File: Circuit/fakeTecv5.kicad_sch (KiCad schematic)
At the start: 70 parts, among them J1 EXTRA, J11 FET1 3,3, J12 FET2 3,3, J13 FET3 3,3, J14 GPS Pins, J16 Encoder Pads, J37 SCL, J38 JST-SH-4, J39 SDA, J40 3.3V, J41 GND, J42 FET1, J43 FET2, J44 FET3, J45 GND, J46 3.3V, J47 GND, J48 GND, J49 GND, J5 I2C Oled screen, J6 FET1 Drain, J7 FET2 Drain, J8 FET3 Drain, J9 JST-PH-2, Q1 AO3400A, Q2 AO3400A, Q3 AO3400A, SW1 Reset, SW2 SW_Push, U1 XB8089D0, U2 HT-RA62, U3 nice!nano v2

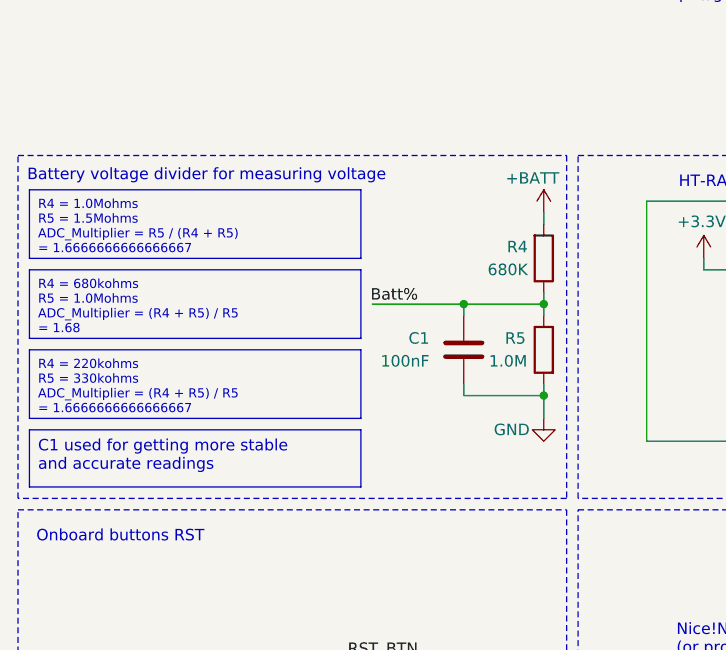
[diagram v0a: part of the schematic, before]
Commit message: improve documentation of battery voltage divider ratio
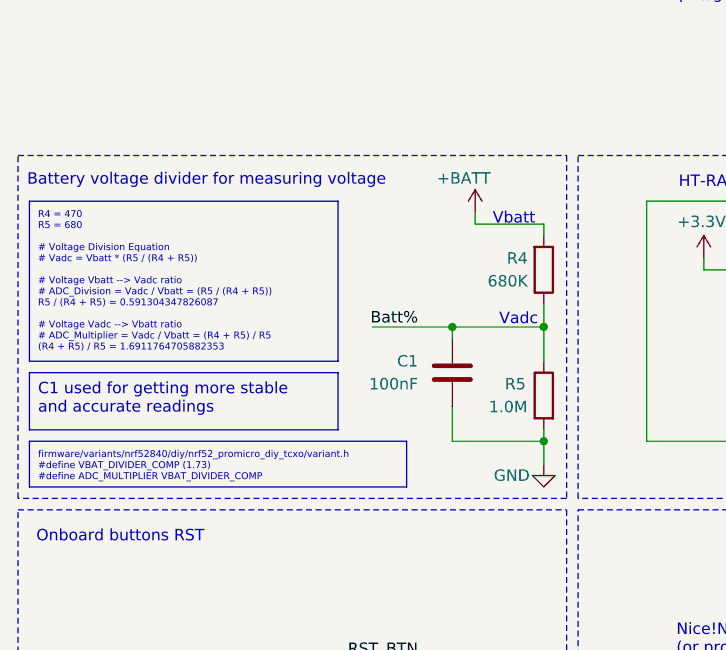
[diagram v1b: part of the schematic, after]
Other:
- note added: "Vadc"
- note added: "Vbatt"
- moved on the sheet: C1, R4, R5

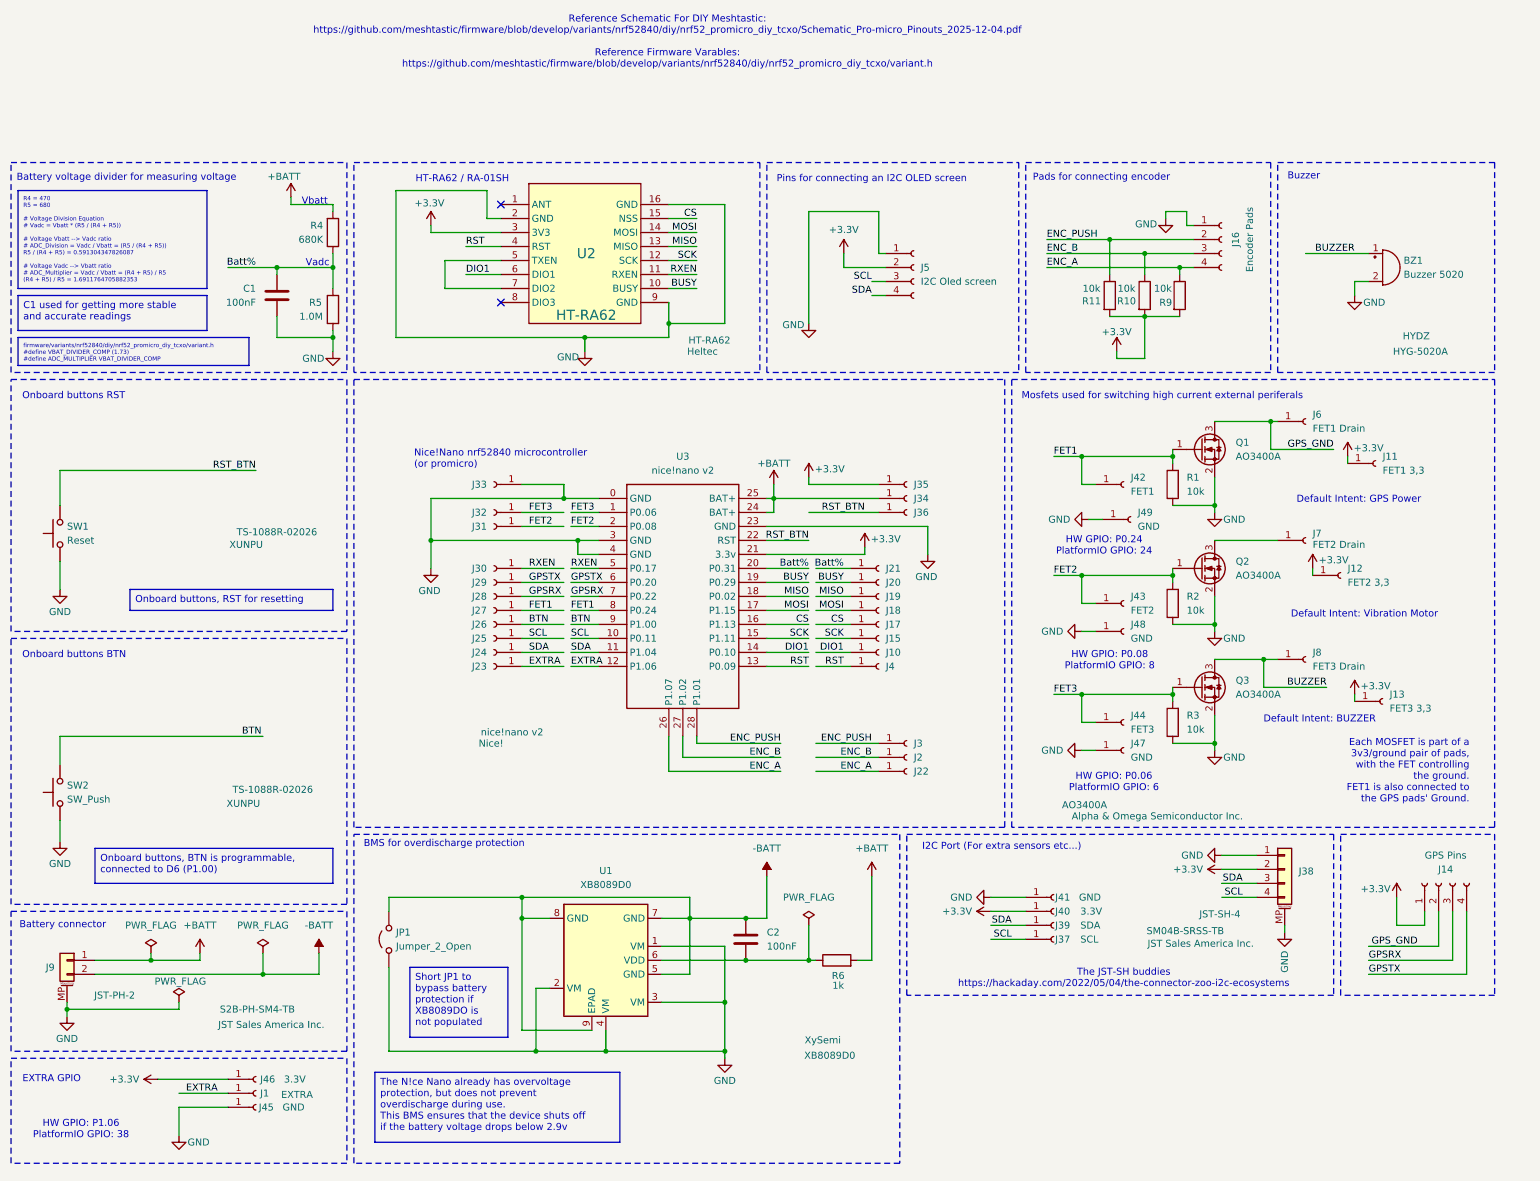
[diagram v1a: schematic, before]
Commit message: bom update and added extra power pads for easier adjustments
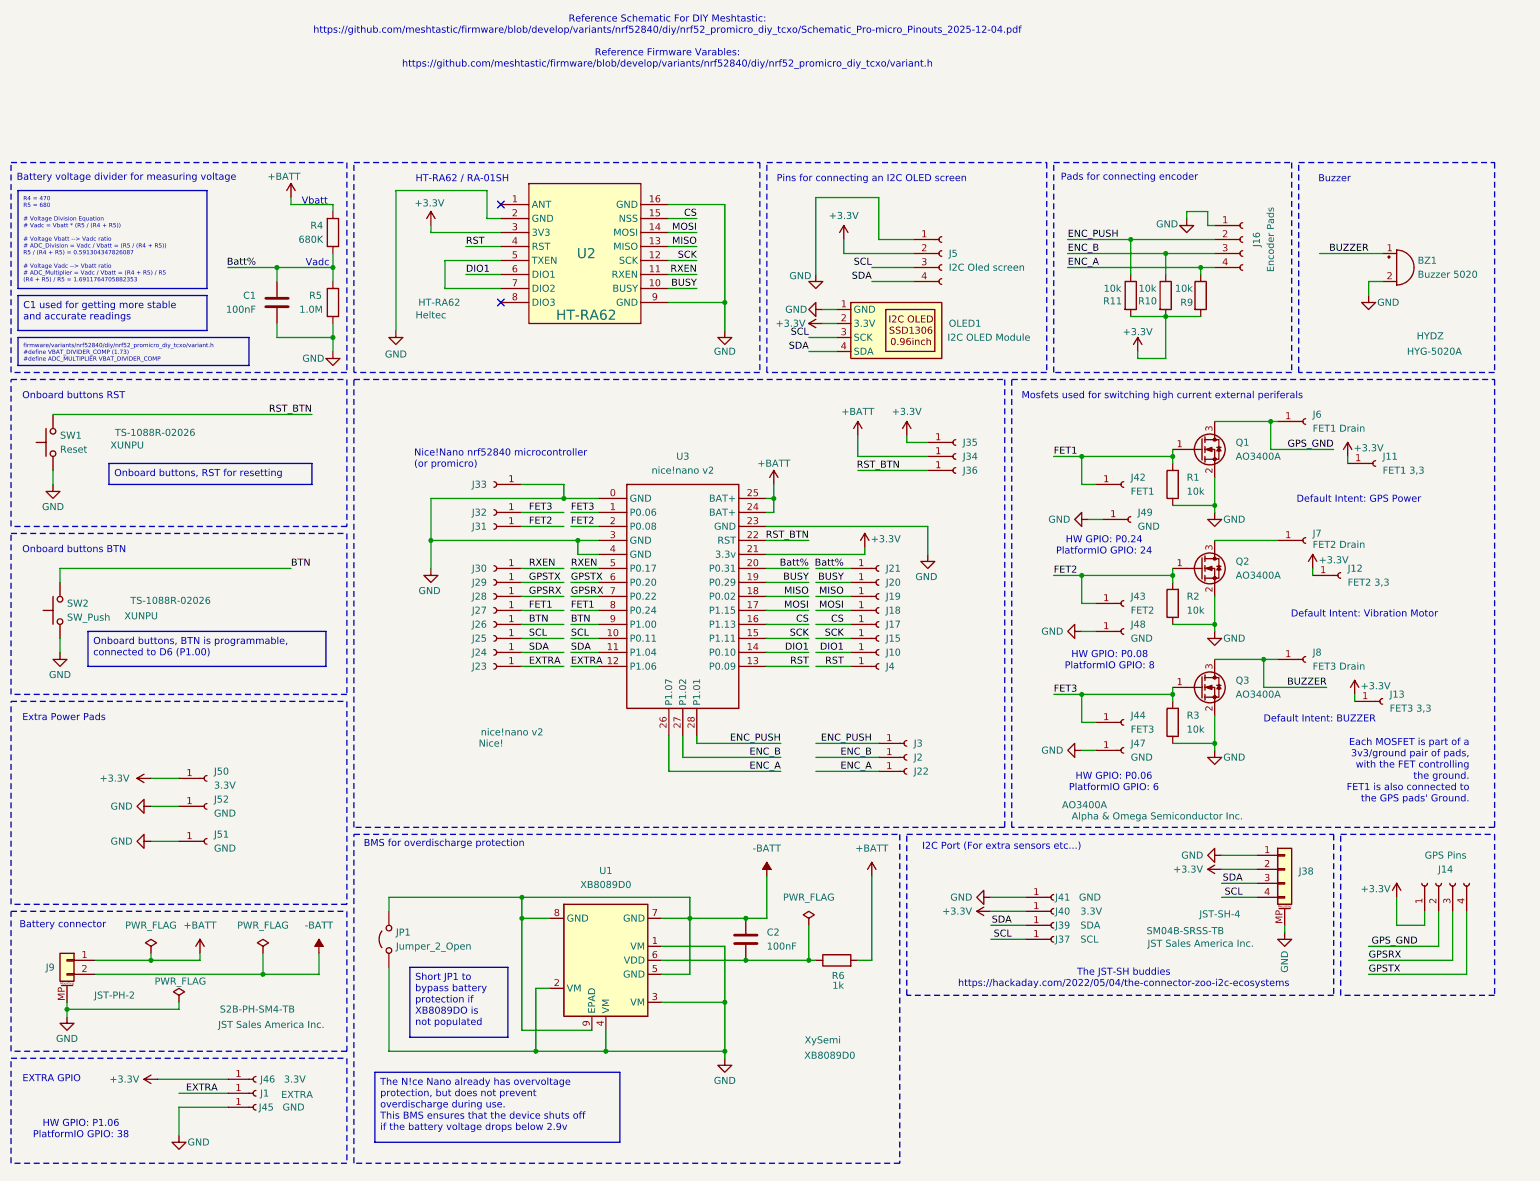
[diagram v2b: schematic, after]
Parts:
- added J50: 3.3V, faketec:SMD_PAD_1x01, symbol Connector:Conn_01x01_Socket
- added J51, J52: GND, faketec:SMD_PAD_1x01, symbol Connector:Conn_01x01_Socket
- added OLED1: I2C OLED Module, symbol faketec:I2C OLED Module
- J5: now left out of the parts list
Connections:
- net +3.3V: now also J50.1 (Pin_1), OLED1.2 (3.3V)
- net GND: now also J51.1 (Pin_1), J52.1 (Pin_1), OLED1.1 (GND)
- net SCL: now also OLED1.3 (SCK)
- net SDA: now also OLED1.4 (SDA)
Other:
- note added: "Extra Power Pads"
- moved on the sheet: BZ1, C1, J16, J34, J35, J36, J5, R10, R11, R5, R9, SW1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

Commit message: updated bom list and schematic with notes on finding all the parts
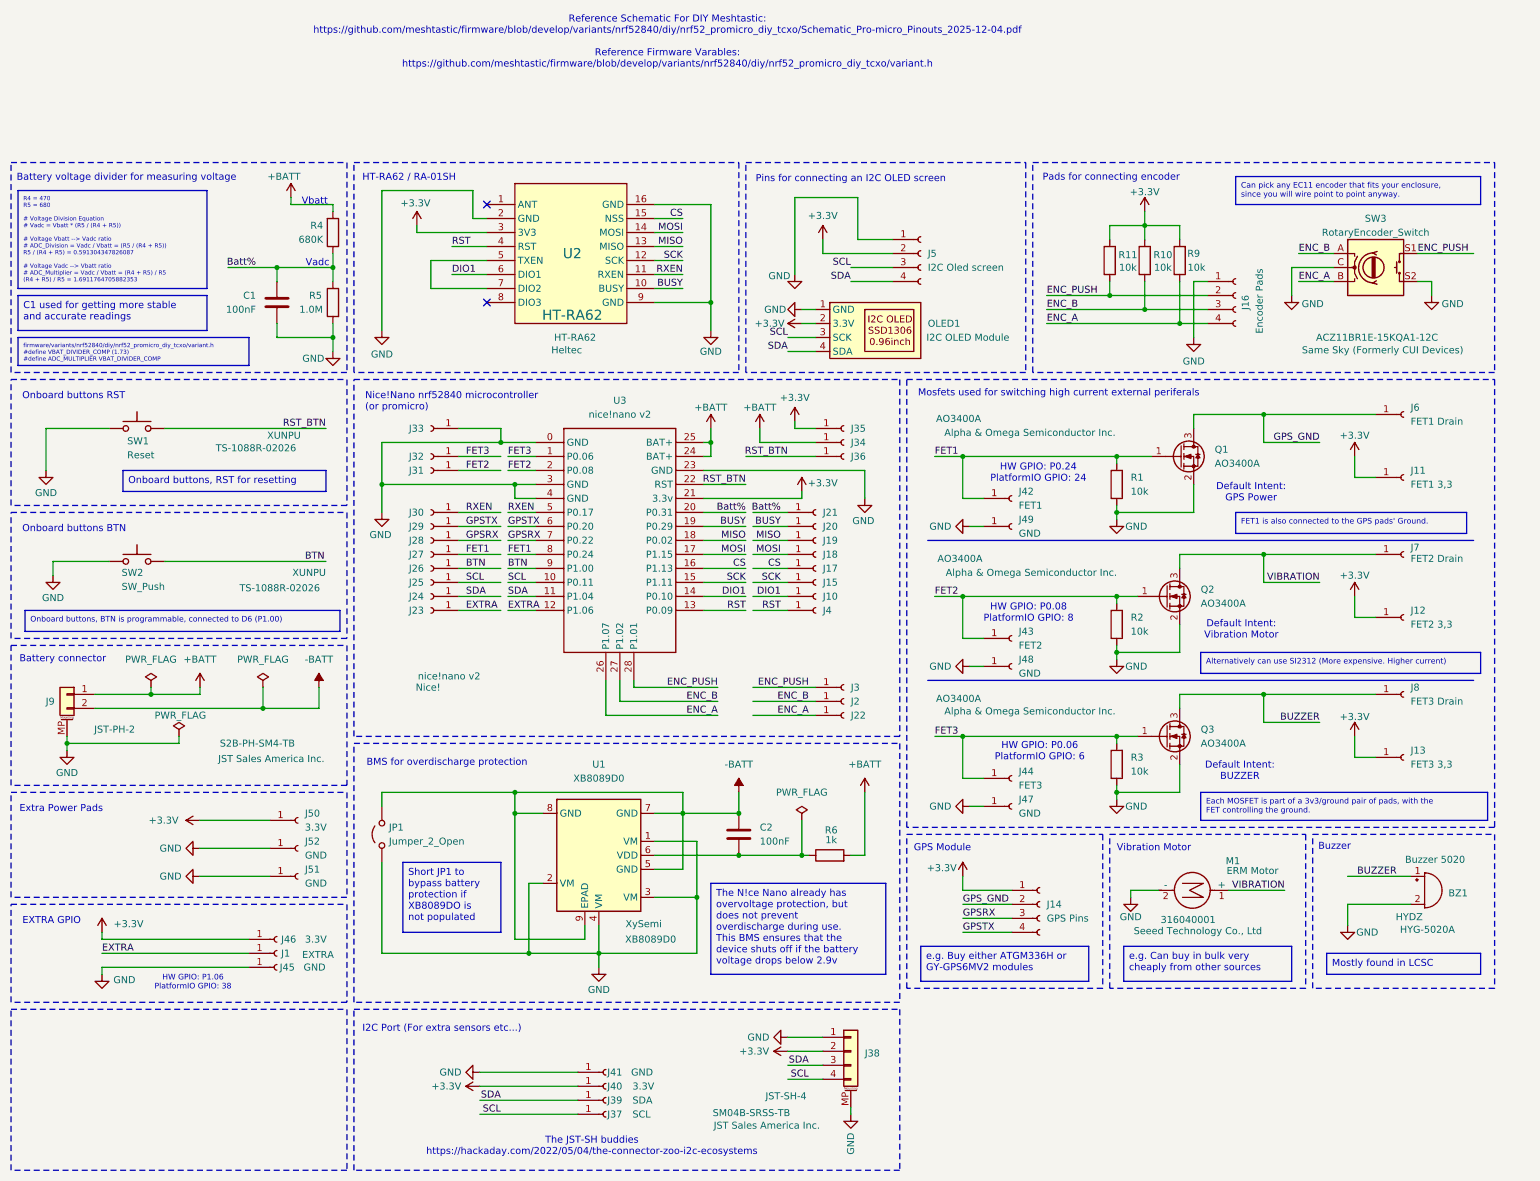
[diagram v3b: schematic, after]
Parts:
- added M1: ERM Motor, symbol Motor:Motor_DC
- added SW3: RotaryEncoder_Switch, symbol Device:RotaryEncoder_Switch
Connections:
- net ENC_A: now also SW3.B
- net ENC_B: now also SW3.A
- net ENC_PUSH: now also SW3.S1
- net GND: now also M1.2 (-), SW3.C, SW3.S2
- net VIBRATION: now reaches J7.1 (Pin_1), Q2.3 (D)
- net VIBRATION: now also M1.1 (+)
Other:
- note added: "GPS Module"
- note added: "Vibration Motor"
- note removed: "Each MOSFET is part of a 3v3/ground pair of pads, with the FET controlling the ground. FET1 is also connected to the GPS pads' Ground."
- moved on the sheet: BZ1, C2, J1, J10, J11, J12, J13, J14, J15, J16, J17, J18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

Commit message: fix schematic typo
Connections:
- net ENC_A: now also SW3.A; no longer SW3.B
- net ENC_B: now also SW3.B; no longer SW3.A
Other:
- note added: "Mosfets used for switching high current external perpherial"
- note removed: "Mosfets used for switching high current external periferals"
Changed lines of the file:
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@@
 		)
 	)
-	(text "Mosfets used for switching high current external periferals"
+	(text "Mosfets used for switching high current external perpherial"
 		(exclude_from_sim no)
 		(at 178.562 55.88 0)
@@
 		)
 	)
-	(label "ENC_B"
-		(at 247.65 30.48 0)
-		(effects
-			(font
-				(size 1.27 1.27)
-			)
-			(justify left bottom)
-		)
-	)
 	(label "SDA"
 		(at 154.94 48.26 180)
@@
 		)
 	)
-	(label "ENC_A"
-		(at 247.65 35.56 0)
+	(label "BUSY"
+		(at 135.89 36.83 180)
 		(effects
 			(font
 				(size 1.27 1.27)
 			)
-			(justify left bottom)
+			(justify right bottom)
 		)
 	)
-	(label "BUSY"
-		(at 135.89 36.83 180)
+	(label "GPSTX"
+		(at 96.52 80.01 0)
 		(effects
 			(font
 				(size 1.27 1.27)
 			)
-			(justify right bottom)
+			(justify left bottom)
 		)
 	)
-	(label "GPSTX"
-		(at 96.52 80.01 0)
+	(label "ENC_A"
+		(at 247.65 30.48 0)
 		(effects
 			(font
@@
 		)
 	)
+	(label "ENC_B"
+		(at 247.65 35.56 0)
+		(effects
+			(font
+				(size 1.27 1.27)
+			)
+			(justify left bottom)
+		)
+	)
